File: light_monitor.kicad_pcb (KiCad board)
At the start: 2 copper layers, 32.9 x 32.9 mm, 33 parts, among them IC1 TSL25911FN, J1 Conn_01x04_Male, J2 Conn_01x03_Male, J3 USB_B_Micro, U1 STM32L432KCUx, U2 STDC14, U3 TPS610986, U4 LDK130PU33R_DFN6, U5 RV-8803-C7, X1 board_lens

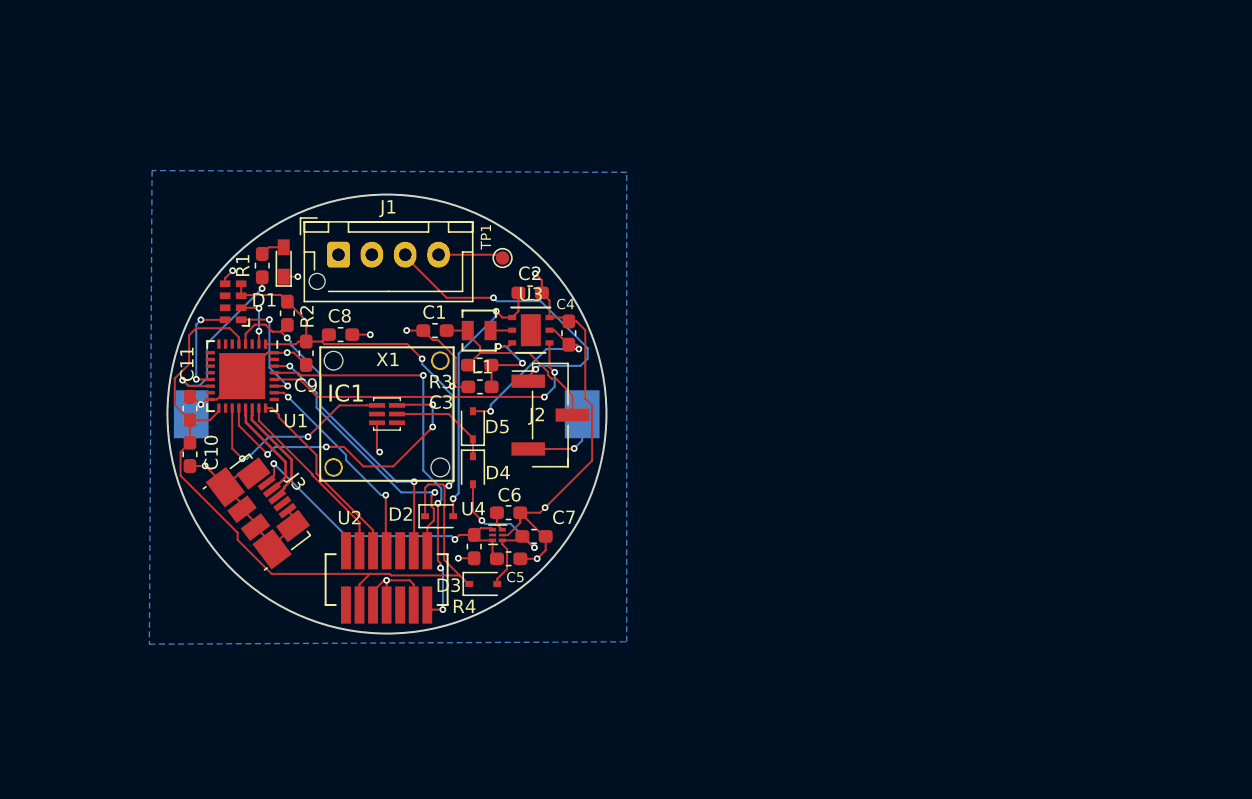
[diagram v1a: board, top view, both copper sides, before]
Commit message: light monitor added
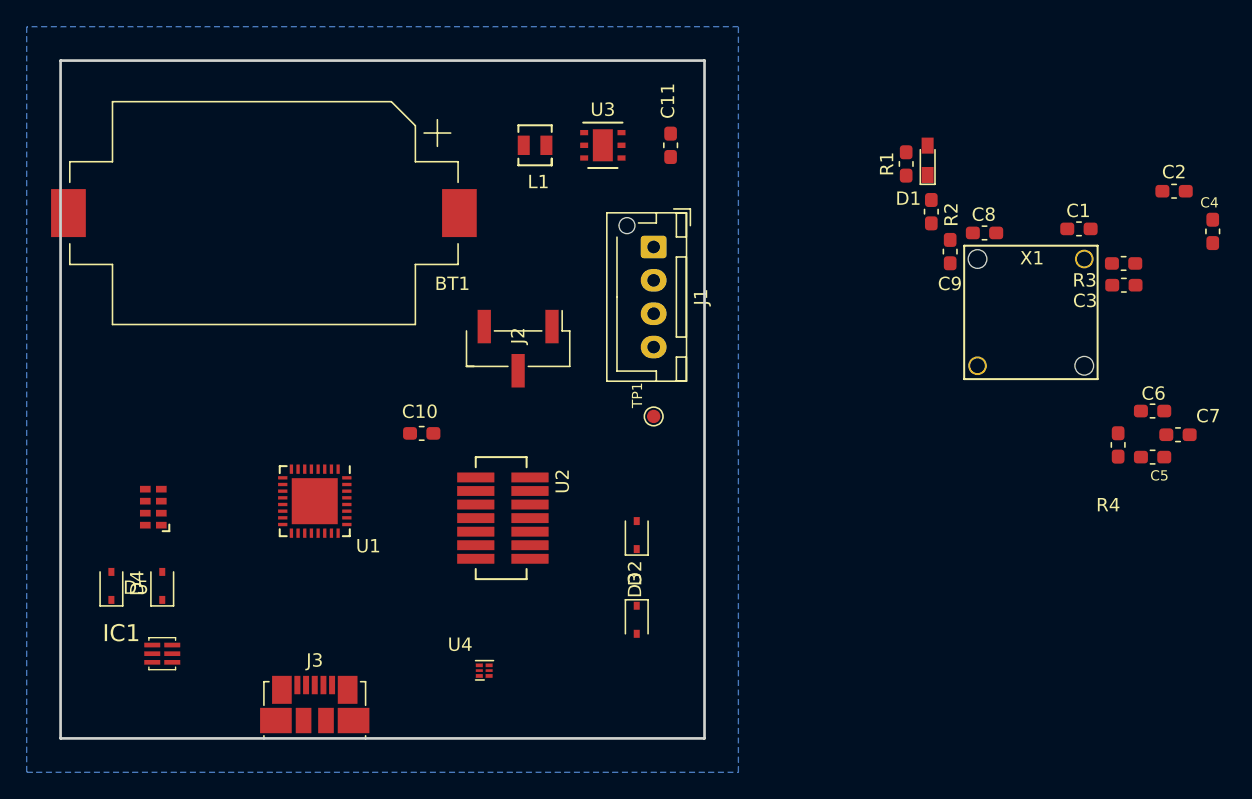
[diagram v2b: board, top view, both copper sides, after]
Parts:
- BT1: moved to F.Cu
- moved C1 48.9 mm to (165.2, 91.4)
- moved C4 48.9 mm to (175.2, 91.5)
- moved C7 48.9 mm to (172.6, 106.8)
- moved D1 48.9 mm to (153.9, 86.2)
- moved R2 48.9 mm to (154.2, 90.1)
- moved R4 48.9 mm to (168.2, 107.5)
- moved X1 48.9 mm to (161.6, 97.6)
- moved C2 48.9 mm to (172.4, 88.5)
- moved C3 48.9 mm to (168.6, 95.6)
- moved C5 48.9 mm to (170.7, 108.5)
- moved C6 48.9 mm to (170.7, 105.0)
- moved C8 48.9 mm to (158.1, 91.7)
- moved C9 48.9 mm to (155.6, 93.1)
- moved R1 48.9 mm to (152.3, 86.5)
- moved R3 48.9 mm to (168.6, 93.9)
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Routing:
- net VDD: track 90.3 -> 0.00 mm, vias 2 -> 0
- net GND: track 84.5 -> 0.00 mm, vias 14 -> 0
- net /TX: track 30.9 -> 0.00 mm, vias 4 -> 0
- net /NRST: track 26.0 -> 0.00 mm, vias 2 -> 0
- net /SW_MODE: track 25.3 -> 0.00 mm, vias 2 -> 0
- net Net-(C5-Pad1): track 23.9 -> 0.00 mm, vias 2 -> 0
- net /sensor_data: track 23.1 -> 0.00 mm, vias 4 -> 0
- net Net-(J1-Pad3): track 22.8 -> 0.00 mm, vias 2 -> 0
- net /RX: track 21.4 -> 0.00 mm, vias 2 -> 0
- net +3V3: track 20.1 -> 0.00 mm, vias 2 -> 0
- net /SWO: track 16.0 -> 0.00 mm, vias 2 -> 0
- net /sensor_clock: track 15.8 -> 0.00 mm, vias 2 -> 0
- net Net-(C1-Pad1): track 14.8 -> 0.00 mm
- net Net-(C7-Pad1): track 14.4 -> 0.00 mm, vias 2 -> 0
- net /SWDCLK: track 14.3 -> 0.00 mm
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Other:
- board size 32.9 x 32.9 mm -> 48.3 x 50.8 mm

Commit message: breakout r001 complete
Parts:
- added J4: Conn_01x03_Male, Connector_PinHeader_2.54mm:PinHeader_1x03_P2.54mm_Vertical, F.Cu at (92.1, 81.9)
- added J5: Conn_01x06_Male, Connector_PinHeader_2.54mm:PinHeader_1x06_P2.54mm_Vertical, F.Cu at (91.4, 109.2)
- added TP2: VIN_SW, TestPoint:TestPoint_Pad_D1.0mm, F.Cu at (126.4, 115.6)
- added TP3: VSW_MAIN, TestPoint:TestPoint_Pad_D1.0mm, F.Cu at (111.8, 123.2)
- added TP4: VSW_SUB, TestPoint:TestPoint_Pad_D1.0mm, F.Cu at (111.8, 114.9)
- added TP5: 3V3_Reg, TestPoint:TestPoint_Pad_D1.0mm, F.Cu at (101.0, 116.2)
- J2: footprint Connector_PinHeader_2.54mm:PinHeader_1x03_P2.54mm_Vertical_SMD_Pin1Left -> Connector_PinHeader_2.54mm:PinHeader_1x03_P2.54mm_Vertical
- moved C6 71.3 mm to (101.0, 119.8), turned to 90 degrees
- moved C5 69.3 mm to (102.9, 122.6), turned to 180 degrees
- moved C7 69.2 mm to (104.4, 118.1)
- moved C4 67.3 mm to (113.7, 118.7), turned to 270 degrees
- moved C2 64.1 mm to (116.8, 120.7), turned to 180 degrees
- moved R4 63.6 mm to (106.0, 121.3)
- moved R2 61.3 mm to (94.6, 104.8), turned to 0 degrees
- moved C8 58.2 mm to (101.6, 105.4), turned to 180 degrees
- moved X1 56.5 mm to (106.7, 84.5)
- moved C3 56.2 mm to (115.6, 114.3)
- moved R3 53.2 mm to (119.4, 114.3), turned to 180 degrees
- moved C1 49.8 mm to (123.2, 118.1), turned to 270 degrees
- moved D1 43.4 mm to (115.6, 106.7), turned to 0 degrees
- moved C9 41.3 mm to (114.3, 92.7)
- moved R1 41.0 mm to (115.6, 104.8), turned to 0 degrees
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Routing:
- net GND: track 0.00 -> 74.6 mm, vias 0 -> 13
- net /sensor_data: track 0.00 -> 65.5 mm, vias 0 -> 4
- net /sensor_clock: track 0.00 -> 62.1 mm, vias 0 -> 6
- net /SW_MODE: track 0.00 -> 45.6 mm, vias 0 -> 4
- net +VSW: track 0.00 -> 44.9 mm, vias 0 -> 2
- net /USB_P: track 0.00 -> 37.2 mm, vias 0 -> 2
- net /rtc_clock: track 0.00 -> 36.0 mm, vias 0 -> 3
- net /rtc_data: track 0.00 -> 35.6 mm, vias 0 -> 3
- net /USB_N: track 0.00 -> 35.2 mm, vias 0 -> 2
- net /oscillator: track 0.00 -> 32.1 mm, vias 0 -> 4
- net VDD: track 0.00 -> 30.7 mm, vias 0 -> 4
- net Net-(J4-Pad2): track 0.00 -> 23.0 mm, vias 0 -> 2
- net /NRST: track 0.00 -> 21.2 mm, vias 0 -> 4
- net Net-(C1-Pad1): track 0.00 -> 19.5 mm
- net Net-(R1-Pad1): track 0.00 -> 16.5 mm, vias 0 -> 2
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- added copper zone on F.Cu, net VDD
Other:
- board text added: "batt"
- board text added: "boot0"
- board text added: "gnd"
- board text added: "lightmon r001"
- board text added: "osc"
- board text added: "pwrmon"
- board text added: "rtc_c"
- board text added: "rtc_d"
- board text added: "sen_c"
- board text added: "sen_d"
- board text added: "vdd"
- board text added: "vin"

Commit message: updated software dev board
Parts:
- added J6: Conn_01x03_Male, Connector_PinHeader_2.54mm:PinHeader_1x03_P2.54mm_Vertical, F.Cu at (105.8, 109.8)
- U3: footprint Package_SON:Texas_PWSON-N6 -> SON50P150X150X80-6N:SON50P150X150X80-6N
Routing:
- net /SW_MODE: track 45.6 -> 46.6 mm
- net /TX: track 15.3 -> 16.2 mm
- net GND: track 74.6 -> 75.5 mm
- net /USB_P: track 37.2 -> 38.0 mm
- net +3V3: track 13.2 -> 14.0 mm
- net Net-(C4-Pad1): track 7.43 -> 8.20 mm
- net Net-(L1-Pad1): track 1.56 -> 2.33 mm
- net Net-(C3-Pad1): track 4.39 -> 5.16 mm
- net /USB_N: track 35.2 -> 35.9 mm
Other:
- board text added: "+"
- board text added: "-"
- board text added: "lightmon r002"
- board text added: "usb"
- board text removed: "lightmon r001"

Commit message: ordered r003 software boards
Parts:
- removed C2, C5: 10uF, Capacitor_SMD:C_0603_1608Metric_Pad1.05x0.95mm_HandSolder
- removed C3: 0.1uF, Capacitor_SMD:C_0603_1608Metric_Pad1.05x0.95mm_HandSolder
- removed C4, C7: 1uF, Capacitor_SMD:C_0603_1608Metric_Pad1.05x0.95mm_HandSolder
- removed C6: 10nF, Capacitor_SMD:C_0603_1608Metric_Pad1.05x0.95mm_HandSolder
- removed D2, D3, D4, D5: D_Schottky, Diode_SMD:D_SOD-323
- removed J4, J6: Conn_01x03_Male, Connector_PinHeader_2.54mm:PinHeader_1x03_P2.54mm_Vertical
- removed L1: 4.7uH, bhimebau_inductor:TDKVLF3025
- removed R3: 400, Resistor_SMD:R_0603_1608Metric_Pad1.05x0.95mm_HandSolder
- removed R4: 100k, Resistor_SMD:R_0603_1608Metric_Pad1.05x0.95mm_HandSolder
- removed TP2: VIN_SW, TestPoint:TestPoint_Pad_D1.0mm
- removed TP3: VSW_MAIN, TestPoint:TestPoint_Pad_D1.0mm
- removed TP4: VSW_SUB, TestPoint:TestPoint_Pad_D1.0mm
- removed TP5: 3V3_Reg, TestPoint:TestPoint_Pad_D1.0mm
- removed U3: TPS610986, SON50P150X150X80-6N:SON50P150X150X80-6N
- removed U4: LDK130PU33R_DFN6, Package_DFN_QFN:DFN-6_1.3x1.2mm_P0.4mm
- added G***: LOGO, boardlogo:board_logo, F.Cu at (119.9, 116.5)
- J3: value USB_B_Micro -> Conn_01x03_Male; footprint Connector_USB:USB_Micro-B_Molex_47346-0001 -> Connector_PinHeader_2.54mm:PinHeader_1x03_P2.54mm_Vertical
- moved C9 16.7 mm to (101.6, 103.5), turned to 180 degrees
- moved C10 16.7 mm to (114.3, 92.7), turned to 270 degrees
- moved J3 10.1 mm to (105.8, 116.9)
- moved C1 8.60 mm to (131.6, 116.4), turned to 90 degrees
- moved J1 7.13 mm to (133.5, 126.0), turned to 180 degrees
- moved TP1 0.62 mm to (120.7, 125.5)
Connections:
- C1 pad 1: Net-(C1-Pad1) -> VDD
- IC1 pad 2: Net-(IC1-Pad2) -> /sensor_int
- IC1 pad 4: Net-(IC1-Pad4) -> (no net)
- IC1 pad 5: +VSW -> VDD
- J1 pad 1: GND -> Net-(J1-Pad1)
- J1 pad 3: Net-(J1-Pad3) -> (no net)
- J1 pad 4: Net-(J1-Pad4) -> GND
- J2 pad 1: Net-(J1-Pad3) -> Net-(J1-Pad2)
- J2 pad 2: Net-(C1-Pad1) -> VDD
- J3 pad 1: Net-(C5-Pad1) -> /rtc_EVI
- J3 pad 2: /USB_N -> /rtc_nINT
- J3 pad 3: /USB_P -> /sensor_int
- TP1 pad 1: Net-(J1-Pad4) -> Net-(J1-Pad1)
- U1 pad 10: Net-(U1-Pad10) -> (no net)
- U1 pad 11: Net-(U1-Pad11) -> /rtc_EVI
- U1 pad 12: Net-(U1-Pad12) -> /rtc_nINT
- U1 pad 15: Net-(U1-Pad15) -> (no net)
- U1 pad 18: Net-(U1-Pad18) -> /sensor_int
- U1 pad 21: /USB_N -> (no net)
- U1 pad 22: /USB_P -> (no net)
- U1 pad 25: Net-(U1-Pad25) -> (no net)
- U1 pad 28: /SW_MODE -> (no net)
- U1 pad 29: /TX -> (no net)
- U1 pad 3: Net-(U1-Pad3) -> (no net)
- U1 pad 30: /RX -> (no net)
- U1 pad 31: Net-(J4-Pad2) -> GND
- U1 pad 6: Net-(U1-Pad6) -> (no net)
- U1 pad 7: Net-(U1-Pad7) -> (no net)
- U1 pad 8: Net-(U1-Pad8) -> /TX
- U1 pad 9: Net-(U1-Pad9) -> /RX
- U2 pad 1: Net-(U2-Pad1) -> (no net)
- U2 pad 10: Net-(U2-Pad10) -> (no net)
- U2 pad 13: /TX -> /RX
- U2 pad 14: /RX -> /TX
- U2 pad 2: Net-(U2-Pad2) -> (no net)
- U2 pad 9: Net-(U2-Pad9) -> (no net)
- U5 pad 6: Net-(U5-Pad6) -> /rtc_nINT
- U5 pad 7: Net-(U5-Pad7) -> /rtc_EVI
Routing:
- net /sensor_int: track 0.00 -> 73.4 mm, vias 0 -> 7
- net /SW_MODE: track 46.6 -> 0.00 mm, vias 4 -> 0
- net +VSW: track 44.9 -> 0.00 mm, vias 2 -> 0
- net /USB_P: track 38.0 -> 0.00 mm, vias 2 -> 0
- net /USB_N: track 35.9 -> 0.00 mm, vias 2 -> 0
- net /rtc_EVI: track 0.00 -> 31.6 mm, vias 0 -> 3
- net /rtc_nINT: track 0.00 -> 31.0 mm, vias 0 -> 3
- net GND: track 75.5 -> 47.9 mm, vias 13 -> 9
- net Net-(J4-Pad2): track 23.0 -> 0.00 mm, vias 2 -> 0
- net Net-(C1-Pad1): track 19.5 -> 0.00 mm
- net Net-(J1-Pad1): track 0.00 -> 14.9 mm
- net Net-(J1-Pad4): track 14.1 -> 0.00 mm
- net +3V3: track 14.0 -> 0.00 mm
- net VDD: track 30.9 -> 44.0 mm, vias 4 -> 7
- net Net-(C5-Pad1): track 9.44 -> 0.00 mm
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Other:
- board text added: "lightmon r003"
- board text added: "rtc_EVI"
- board text added: "rtc_nINT"
- board text added: "sensor_int"
- board text removed: "+"
- board text removed: "-"
- board text removed: "boot0"
- board text removed: "lightmon r002"
- board text removed: "usb"
- board text removed: "vdd"

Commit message: breakout completed
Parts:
- removed G***: LOGO, boardlogo:board_logo
- added J4: Conn_01x02_Male, Connector_PinHeader_2.54mm:PinHeader_1x02_P2.54mm_Vertical, F.Cu at (102.8, 109.7)
- added J6: Conn_01x02_Male, Connector_PinHeader_2.54mm:PinHeader_1x02_P2.54mm_Vertical, F.Cu at (92.5, 88.1)
- added J7: Conn_01x02_Male, Connector_PinHeader_2.54mm:PinHeader_1x02_P2.54mm_Vertical, F.Cu at (113.9, 87.6)
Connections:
- C10 pad 1: VDD -> /uC_VDD
- C11 pad 1: VDD -> /uC_VDD
- C8 pad 1: VDD -> /uC_VDD
- C9 pad 1: VDD -> /uC_VDD
- IC1 pad 5: VDD -> /SENSOR_VDD
- R2 pad 1: VDD -> /uC_VDD
- U1 pad 1: VDD -> /uC_VDD
- U1 pad 17: VDD -> /uC_VDD
- U1 pad 21: (no net) -> /sensor_power
- U1 pad 5: VDD -> /uC_VDD
- U2 pad 3: VDD -> /uC_VDD
- U5 pad 3: VDD -> /RTC_VDD
- U5 pad 4: VDD -> /RTC_VDD
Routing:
- net /uC_VDD: track 0.00 -> 66.1 mm, vias 0 -> 4
- net VDD: track 44.0 -> 3.07 mm, vias 7 -> 0
- net /sensor_power: track 0.00 -> 14.8 mm, vias 0 -> 2
- net /SENSOR_VDD: track 0.00 -> 6.78 mm
- net /RTC_VDD: track 0.00 -> 3.75 mm
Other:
- board text added: "lightmon r004"
- board text removed: "lightmon r003"

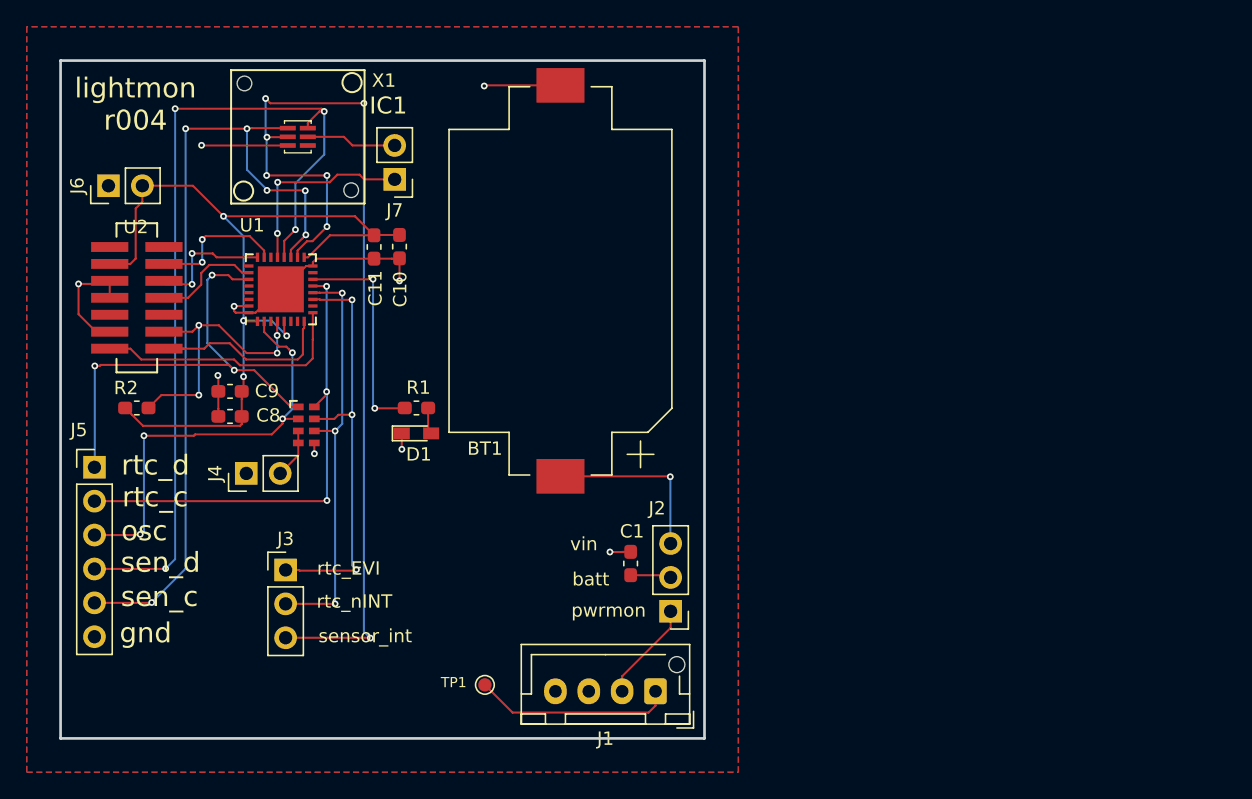
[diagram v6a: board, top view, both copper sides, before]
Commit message: r004 breakout created and routed.
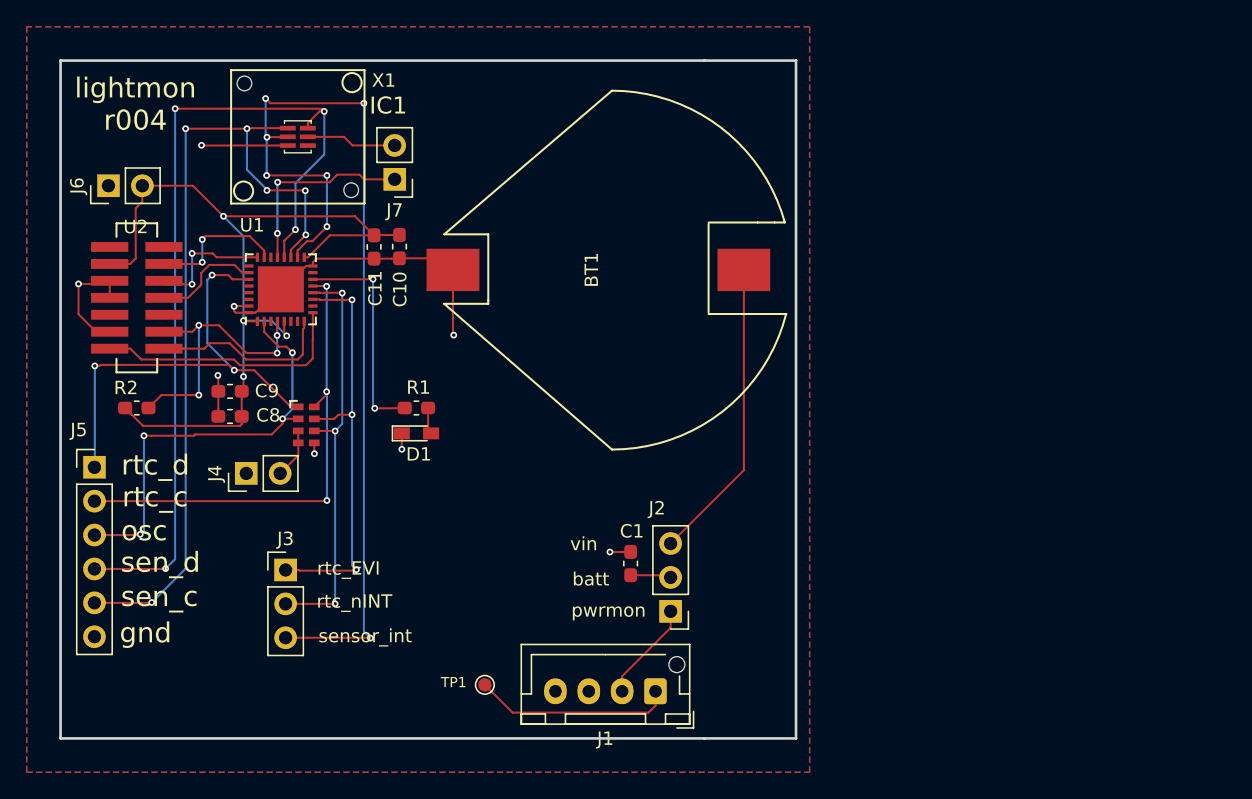
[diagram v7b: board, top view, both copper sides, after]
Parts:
- BT1: footprint Battery:BatteryHolder_Keystone_1060_1x2032 -> bhimebau_battery:Keystone_1091TR
- moved BT1 2.96 mm to (129.2, 94.4), turned to 270 degrees
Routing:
- net Net-(BT1-Pad1): track 13.3 -> 22.8 mm, vias 1 -> 0
- net GND: track 47.9 -> 49.8 mm, vias 9 -> 8
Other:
- board size 48.3 x 50.8 mm -> 55.1 x 50.8 mm
